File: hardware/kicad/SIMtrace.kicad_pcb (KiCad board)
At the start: 2 copper layers, 85.9 x 54.2 mm, 73 parts, among them IC1 FPF2109, IC2 AP7332, IC3 MCU, IC4 CB3Q3244, J1 USB, J2 SERIAL, P1 JTAG, P2 DEBUG, P3 FFC, P4 SIM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

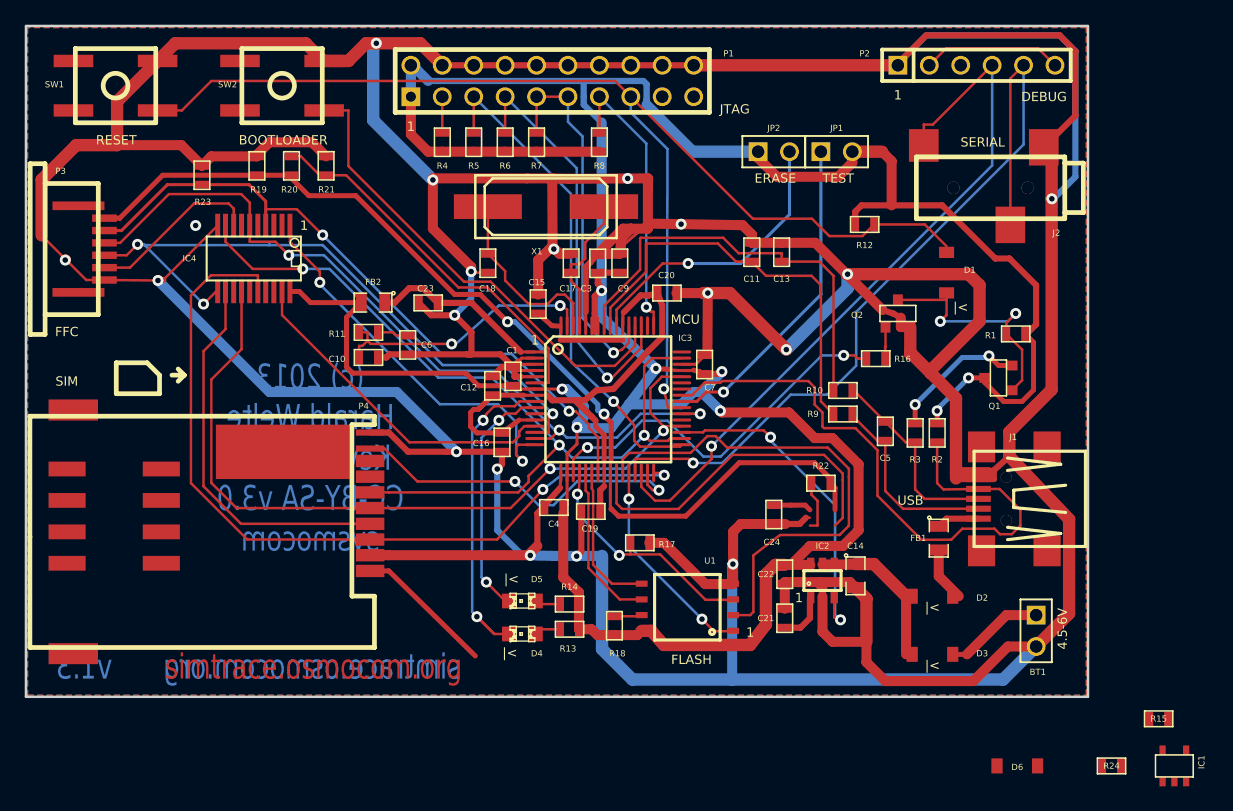
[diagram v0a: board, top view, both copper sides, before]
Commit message: new components placed and routed
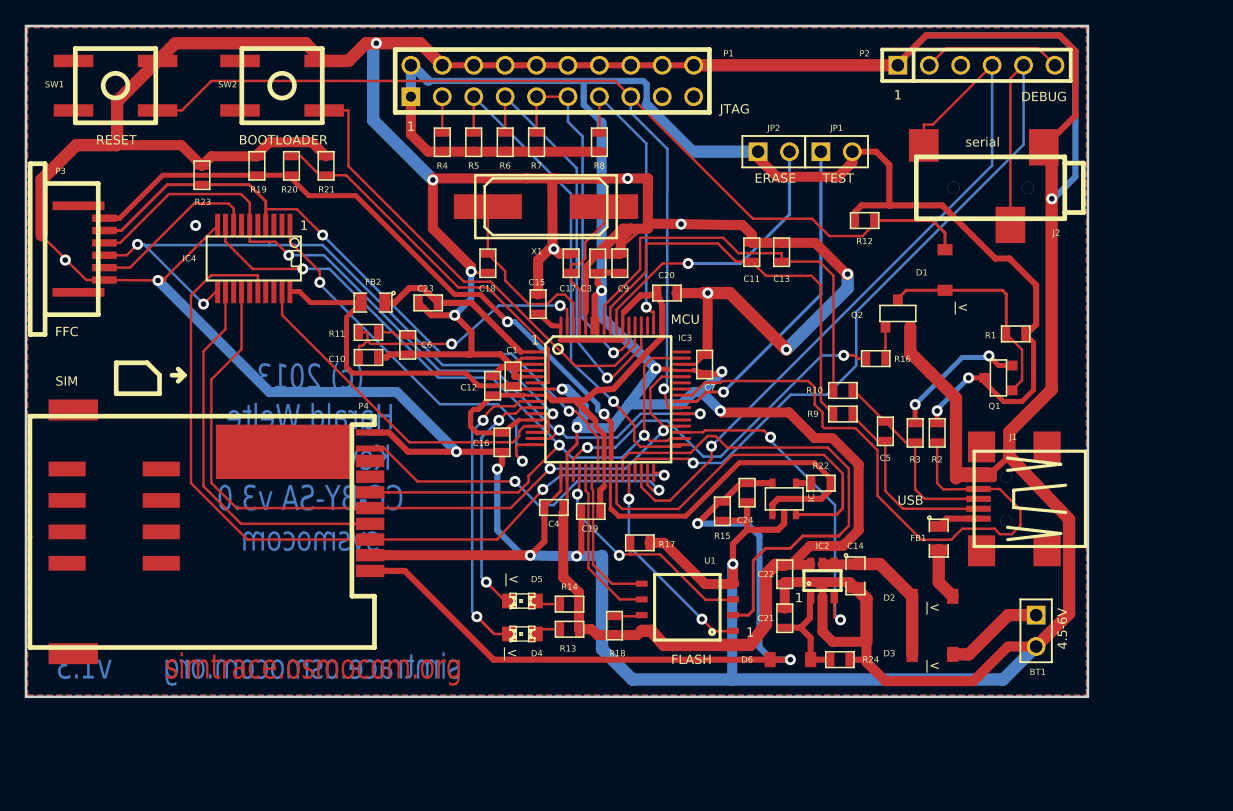
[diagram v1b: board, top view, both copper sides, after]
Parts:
- J2: value SERIAL -> serial
- moved R15 39.1 mm to (93.0, 128.0), turned to 270 degrees
- moved IC1 38.2 mm to (98.0, 127.0)
- moved R24 23.6 mm to (102.5, 140.0)
- moved D6 20.3 mm to (98.5, 140.0)
- moved C24 2.79 mm to (95.0, 126.5)
- moved R12 0.32 mm to (104.5, 104.5)
- moved D1 0.25 mm to (111.0, 108.5), turned to 270 degrees
- turned D2 to 0 degrees
- turned D3 to 0 degrees
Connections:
- BT1 pad 1: N-0000036 (its old number) -> N-0000034
- C14 pad 1: N-0000061 (its old number) -> N-0000059
- D1 pad 1: /UDP_PUP -> //RESET
- D1 pad 2: //RESET -> /UDP_PUP
- D2 pad 1: /USBVCC -> N-0000059
- D2 pad 2: N-0000061 (its old number) -> /USBVCC
- D3 pad 1: N-0000036 (its old number) -> N-0000059
- D3 pad 2: N-0000061 (its old number) -> N-0000034
- D6 pad 1: N-0000019 -> /VCC_SIM
- D6 pad 2: /VCC_SIM -> N-0000019
- IC2 pad 4: N-0000061 (its old number) -> N-0000059
- IC2 pad 5: N-0000061 (its old number) -> N-0000059
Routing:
- net /VCC_SIM: track 24.2 -> 61.7 mm, vias 0 -> 2
- net GND: track 616.0 -> 591.7 mm
- net N-0000059: track 0.00 -> 13.0 mm
- net N-0000061 (its old number): track 12.6 -> 0.00 mm
- net N-0000034: track 0.00 -> 8.06 mm
- net N-0000036 (its old number): track 7.57 -> 0.00 mm
- net 3V3: track 295.8 -> 290.8 mm
- net N-0000019: track 4.12 -> 8.65 mm
- net /VCC_PHONE: track 82.3 -> 86.5 mm
- net N-0000031: track 4.25 -> 1.25 mm
- net /VCC_FWD: track 27.8 -> 30.2 mm
- net /UDP_PUP: track 19.7 -> 17.9 mm, vias 2 -> 0
- net //RESET: track 98.7 -> 99.6 mm

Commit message: MCU pin 48 used to identify v1.3 by putting it to ground (with internal pull-up)
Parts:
- J2: value serial -> SERIAL
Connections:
- IC3 pad 48: (no net) -> GND
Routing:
- net GND: track 591.7 -> 593.6 mm
